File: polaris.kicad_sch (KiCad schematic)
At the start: 17 parts, among them J101 Conn_01x02, J102 Screw_Terminal_01x02, J103 Screw_Terminal_01x02, J104 Screw_Terminal_01x02, J105 Screw_Terminal_01x02, J106 Screw_Terminal_01x02, J107 Screw_Terminal_01x02, J108 Screw_Terminal_01x03, J109 Screw_Terminal_01x03, J110 Screw_Terminal_01x03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

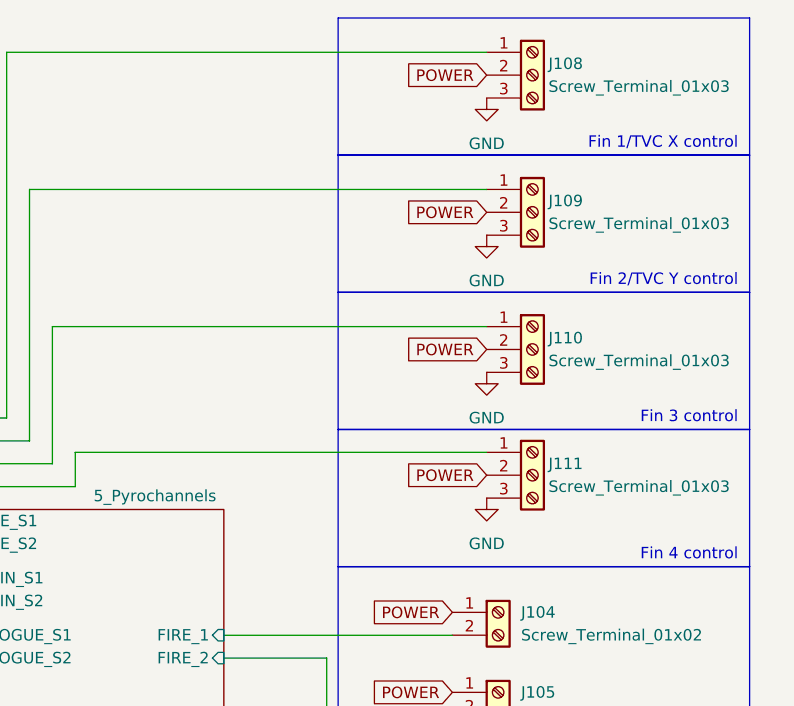
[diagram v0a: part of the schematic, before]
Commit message: Corrected power section for the billionth time Added programming notes
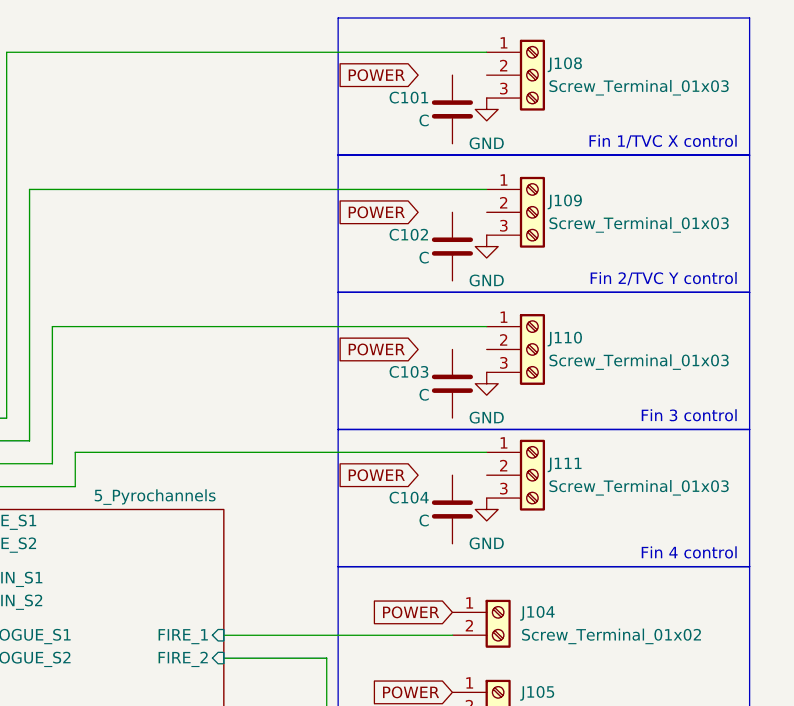
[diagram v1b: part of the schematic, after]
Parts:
- added C101, C102, C103, C104: C, symbol Device:C
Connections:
- net POWER: no longer J108.2 (Pin_2), J109.2 (Pin_2), J110.2 (Pin_2), J111.2 (Pin_2)

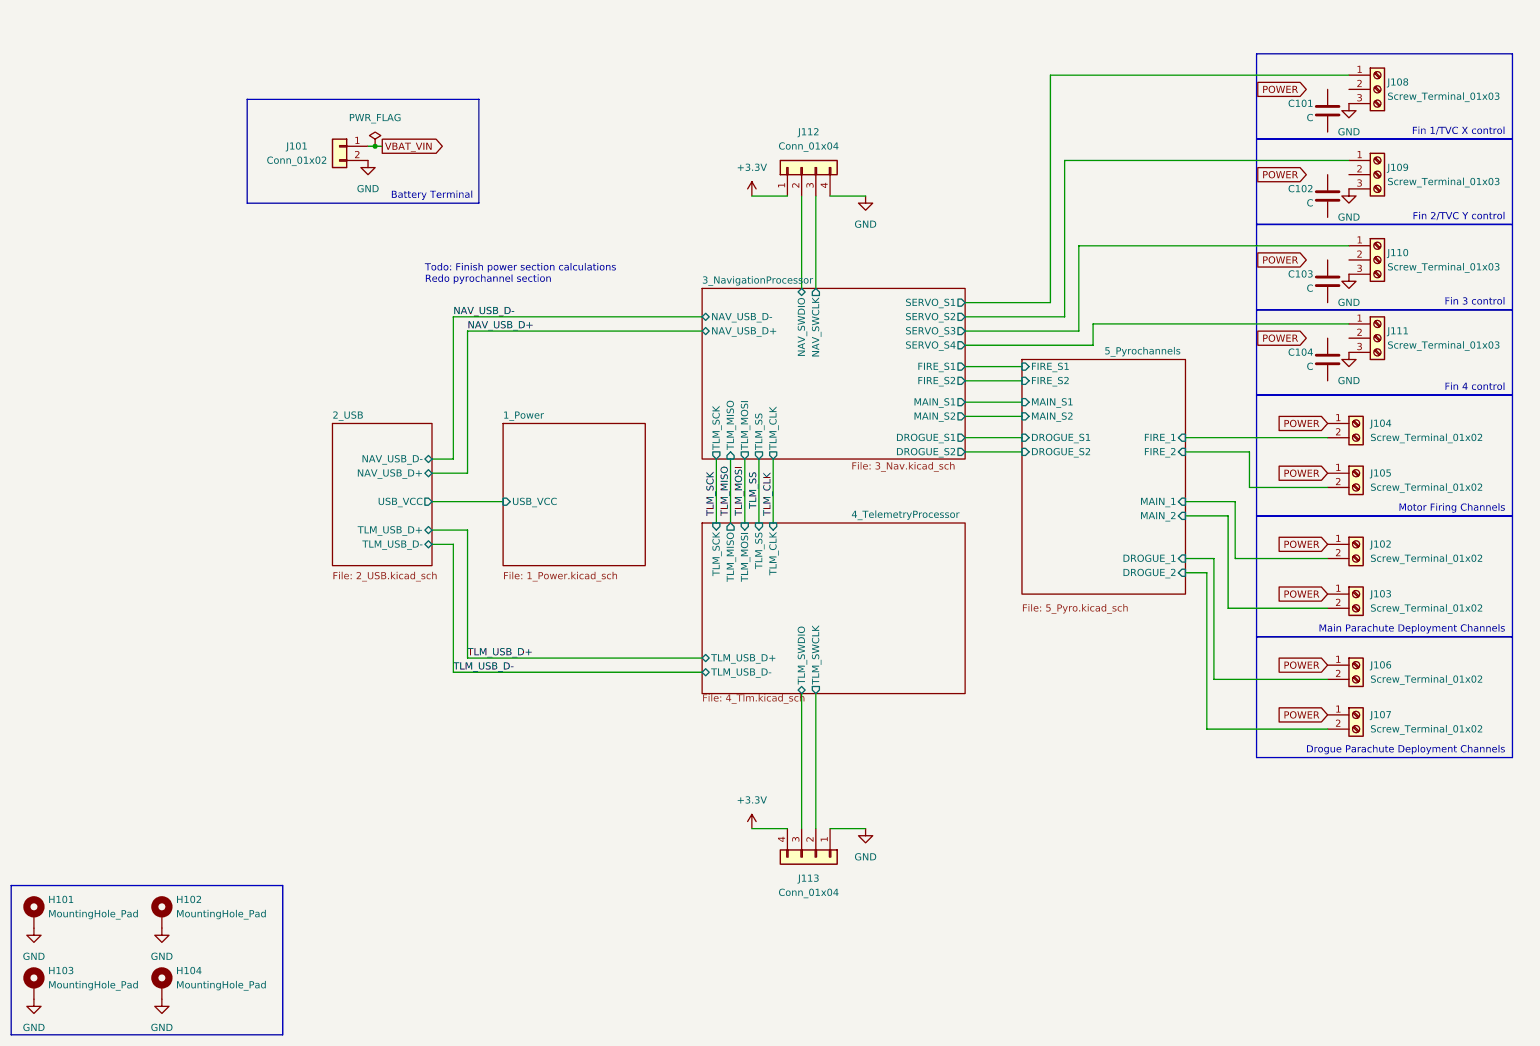
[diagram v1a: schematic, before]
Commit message: Added hardware switch for active control Also added a coupling capacitor between receptacle shells and reference ground Added some more notes
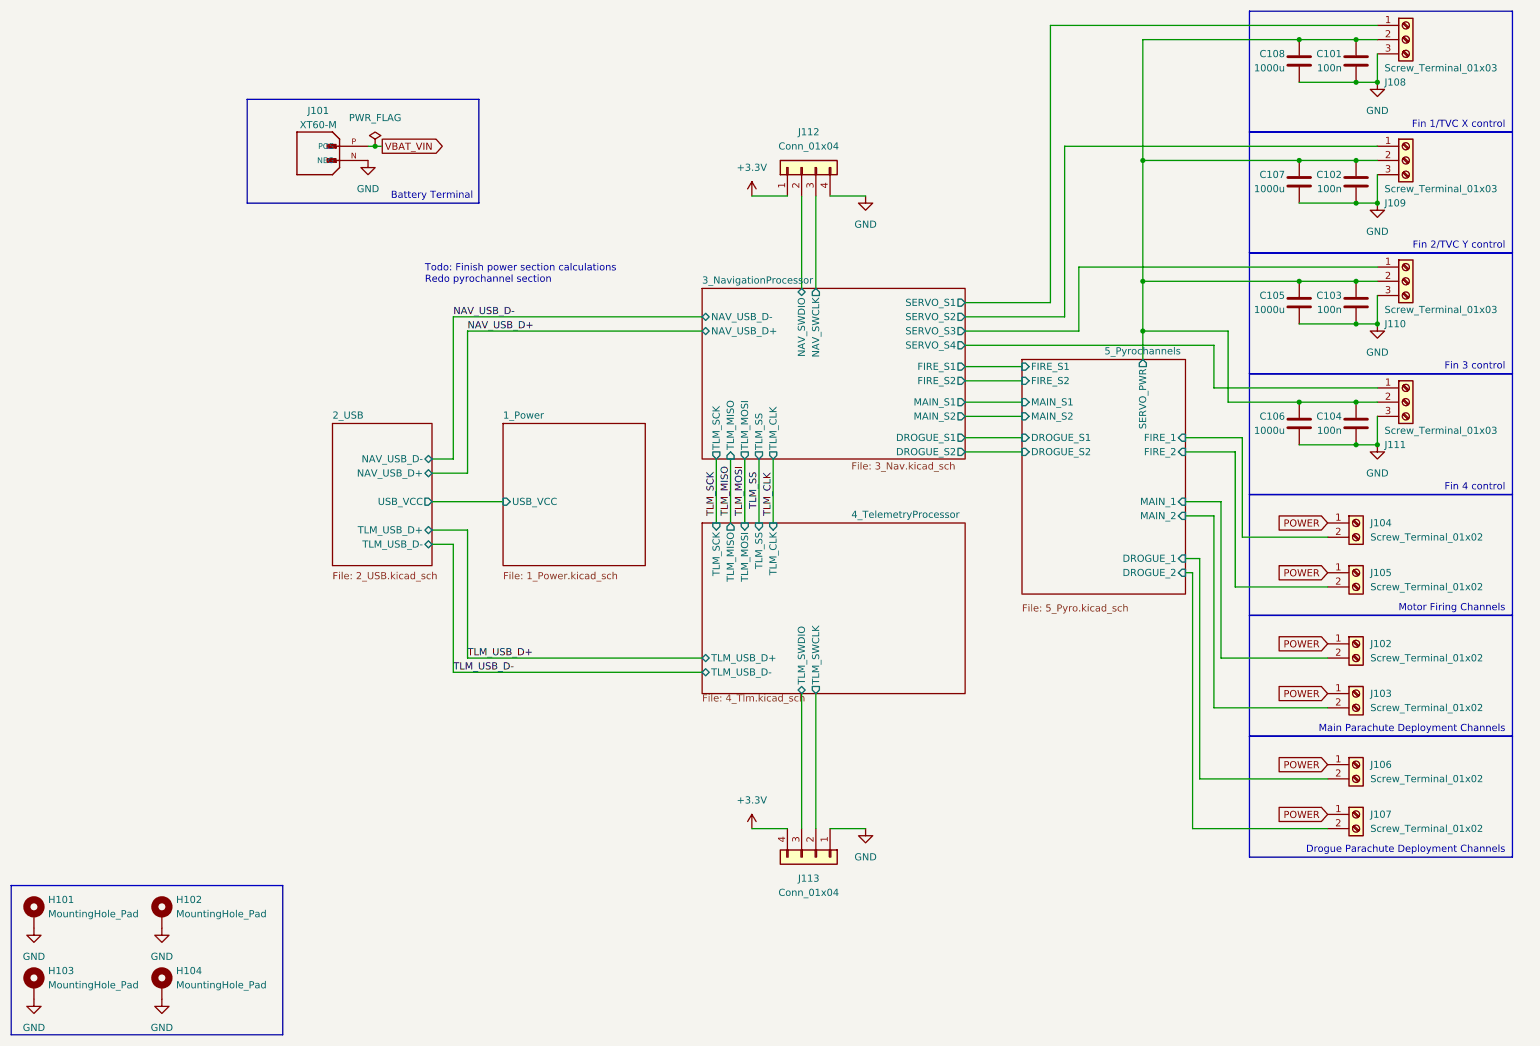
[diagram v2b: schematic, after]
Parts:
- removed J101: Conn_01x02, Connector_AMASS:AMASS_XT60-M_1x02_P7.20mm_Vertical, symbol Connector_Generic:Conn_01x02
- added C105, C106, C107, C108: 1000u, symbol Device:C
- added J101: XT60-M, Connector_AMASS:AMASS_XT60-M_1x02_P7.20mm_Vertical, symbol Polaris_symbols:XT60-M
- C101, C102, C103, C104: value C -> 100n
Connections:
- net GND: now also C101.2, C102.2, C103.2, C104.2, C105.2, C106.2, C107.2, C108.2, J101.N (NEG)
- net VBAT_VIN: now also J101.P (POS)
- net 5_Pyrochannels/SERVO_PWR: now reaches J109.2 (Pin_2)
- net 5_Pyrochannels/SERVO_PWR: now also C101.1, C102.1, C103.1, C104.1, J108.2 (Pin_2), J110.2 (Pin_2), J111.2 (Pin_2), C105.1, C106.1, C107.1, C108.1
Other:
- sheet 5_Pyrochannels ports: added SERVO_PWR; removed none
- title: (none) -> Polaris
- moved on the sheet: C101, C102, C103, C104, J102, J103, J104, J105, J106, J107, J108, J109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

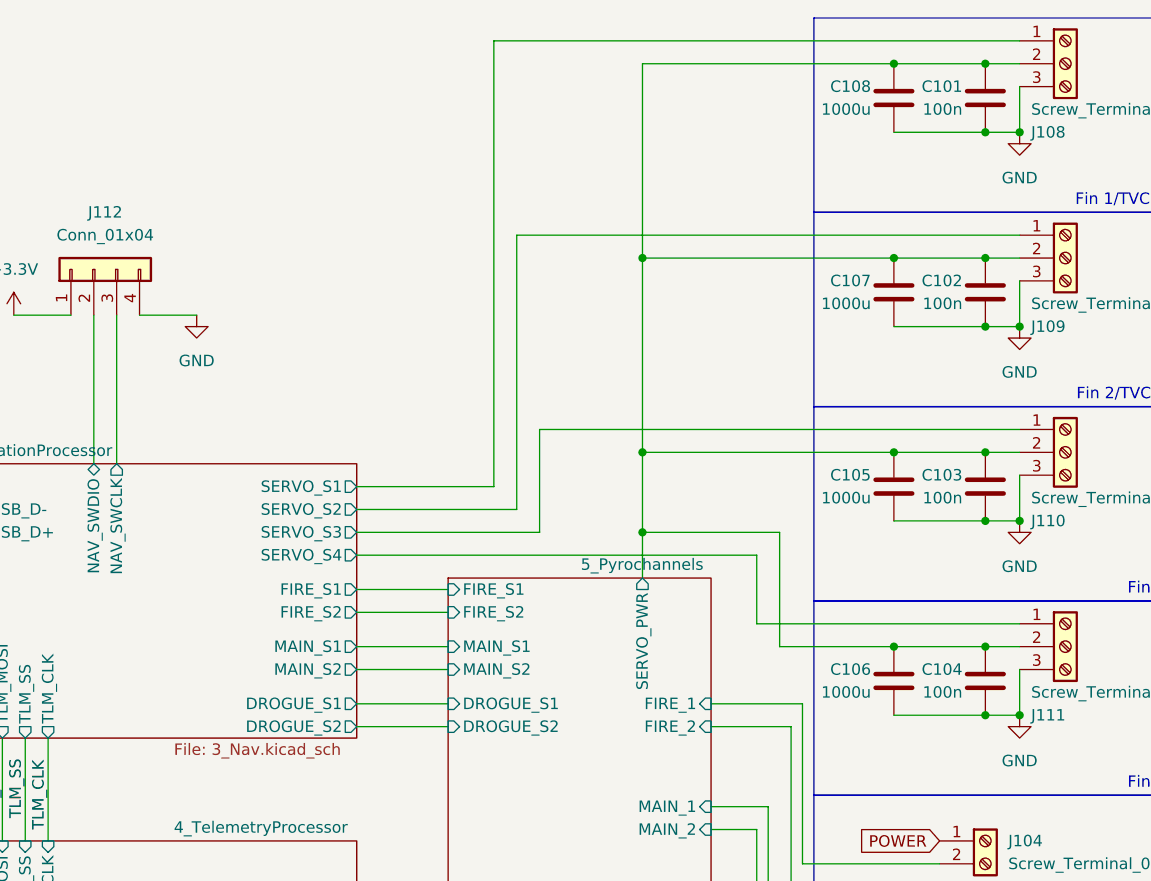
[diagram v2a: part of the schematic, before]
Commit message: Used custom buzzer footprint because why not
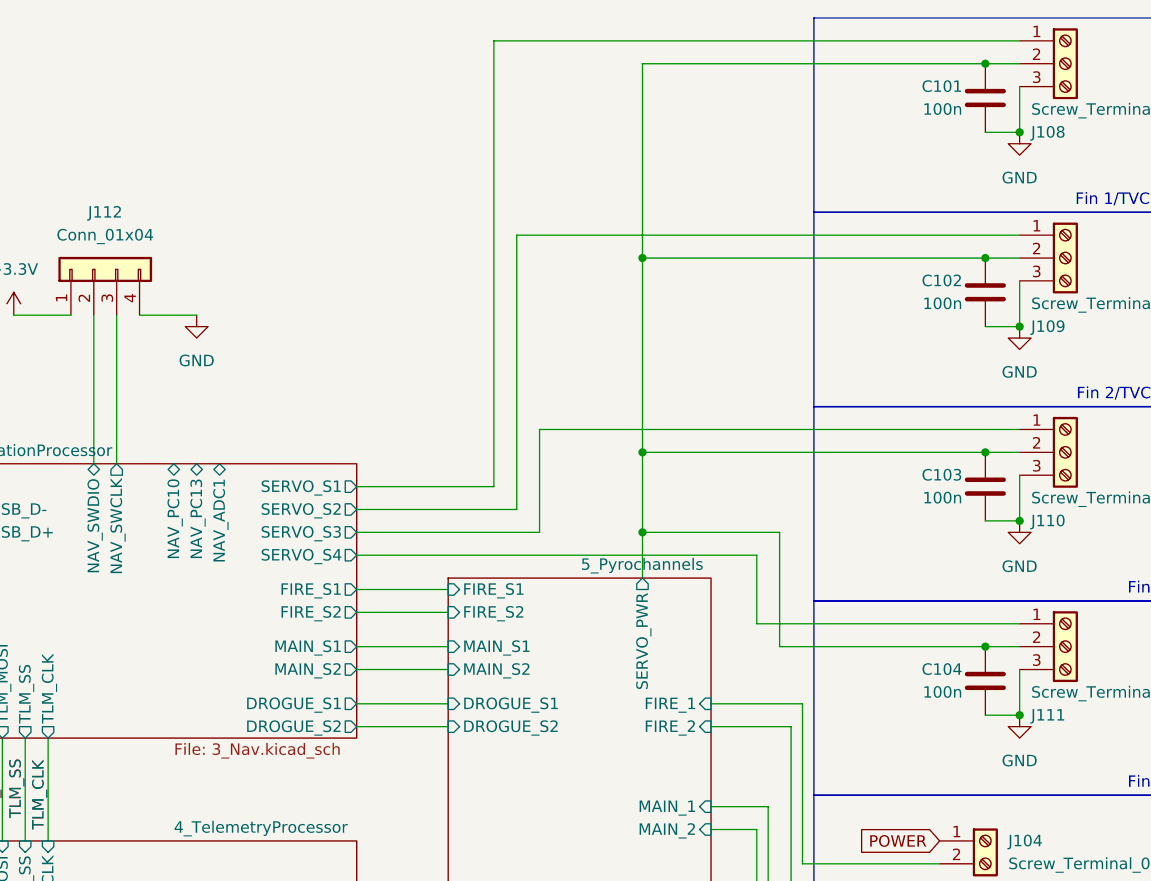
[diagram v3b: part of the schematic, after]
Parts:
- removed C105, C106, C107, C108: 1000u, symbol Device:C
- C101, C102, C103, C104: footprint (none) -> Capacitor_SMD:C_0603_1608Metric
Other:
- sheet 3_NavigationProcessor ports: added NAV_ADC1, NAV_PC10, NAV_PC13; removed none

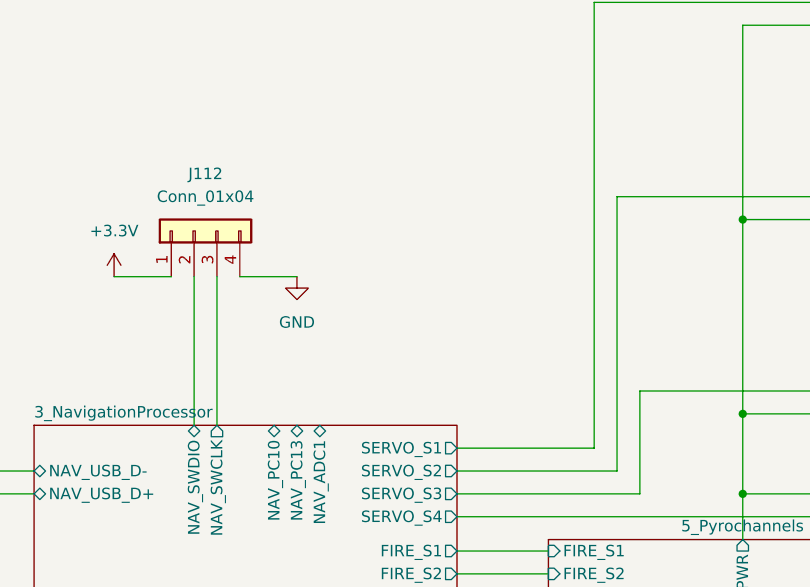
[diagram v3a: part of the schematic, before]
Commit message: Broke out the remaining GPIO pins of NAV
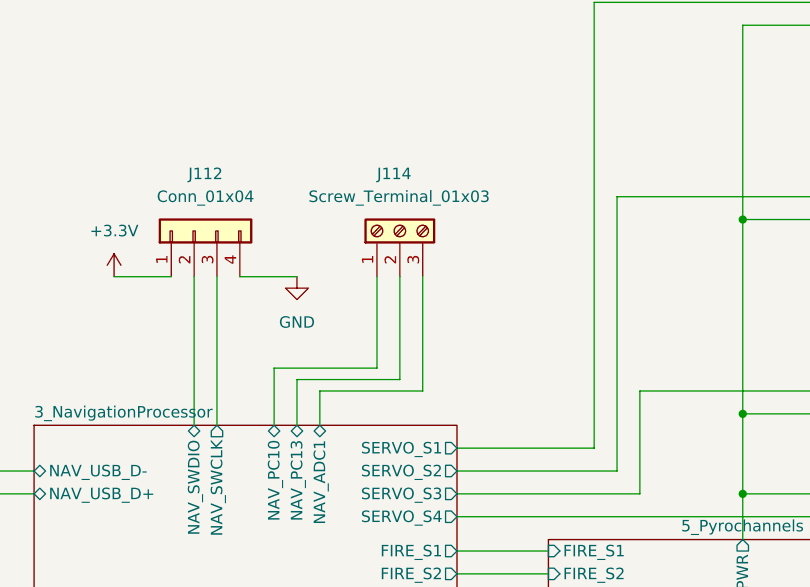
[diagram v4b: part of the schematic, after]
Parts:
- added J114: Screw_Terminal_01x03, TerminalBlock:TerminalBlock_Xinya_XY308-2.54-3P_1x03_P2.54mm_Horizontal, symbol Connector:Screw_Terminal_01x03
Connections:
- net 3_NavigationProcessor/NAV_ADC1: now also J114.3 (Pin_3)
- net 3_NavigationProcessor/NAV_PC10: now also J114.1 (Pin_1)
- net 3_NavigationProcessor/NAV_PC13: now also J114.2 (Pin_2)
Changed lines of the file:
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@@
 	(wire
 		(pts
+			(xy 163.83 57.15) (xy 175.26 57.15)
+		)
+		(stroke
+			(width 0)
+			(type default)
+		)
+	)
+	(wire
+		(pts
 			(xy 92.71 68.58) (xy 92.71 93.98)
 		)
@@
 	(wire
 		(pts
+			(xy 166.37 58.42) (xy 177.8 58.42)
+		)
+		(stroke
+			(width 0)
+			(type default)
+		)
+	)
+	(wire
+		(pts
 			(xy 78.74 38.1) (xy 80.01 38.1)
 		)
@@
 	(wire
 		(pts
+			(xy 168.91 59.69) (xy 180.34 59.69)
+		)
+		(stroke
+			(width 0)
+			(type default)
+		)
+	)
+	(wire
+		(pts
 			(xy 204.47 59.69) (xy 257.81 59.69)
 		)
@@
 	(wire
 		(pts
+			(xy 168.91 63.5) (xy 168.91 59.69)
+		)
+		(stroke
+			(width 0)
+			(type default)
+		)
+	)
+	(wire
+		(pts
 			(xy 223.52 101.6) (xy 229.87 101.6)
 		)
@@
 	(wire
 		(pts
+			(xy 177.8 46.99) (xy 177.8 58.42)
+		)
+		(stroke
+			(width 0)
+			(type default)
+		)
+	)
+	(wire
+		(pts
 			(xy 88.9 101.6) (xy 101.6 101.6)
 		)
@@
 	(wire
 		(pts
+			(xy 163.83 63.5) (xy 163.83 57.15)
+		)
+		(stroke
+			(width 0)
+			(type default)
+		)
+	)
+	(wire
+		(pts
 			(xy 146.05 160.02) (xy 152.4 160.02)
 		)
@@
 	(wire
 		(pts
+			(xy 180.34 59.69) (xy 180.34 46.99)
+		)
+		(stroke
+			(width 0)
+			(type default)
+		)
+	)
+	(wire
+		(pts
 			(xy 254 19.05) (xy 257.81 19.05)
 		)
@@
 	(wire
 		(pts
+			(xy 166.37 63.5) (xy 166.37 58.42)
+		)
+		(stroke
+			(width 0)
+			(type default)
+		)
+	)
+	(wire
+		(pts
 			(xy 184.15 77.47) (xy 194.31 77.47)
 		)
@@
 	(wire
 		(pts
+			(xy 175.26 46.99) (xy 175.26 57.15)
+		)
+		(stroke
+			(width 0)
+			(type default)
+		)
+	)
+	(wire
+		(pts
 			(xy 95.25 106.68) (xy 95.25 129.54)
 		)
@@
 					(unit 1)
 				)
+			)
+		)
+	)
+	(symbol
+		(lib_id "Connector:Screw_Terminal_01x03")
+		(at 177.8 41.91 90)
+		(unit 1)
+		(body_style 1)
+		(exclude_from_sim no)
+		(in_bom yes)
+		(on_board yes)
+		(in_pos_files yes)
+		(dnp no)
+		(property "Reference" "J114"
+			(at 175.26 35.56 90)
+			(show_name no)
+			(do_not_autoplace no)
+			(effects
+				(font
+					(size 1.27 1.27)
+				)
+				(justify right)
+			)
+		)
+		(property "Value" "Screw_Terminal_01x03"
+			(at 167.64 38.1 90)
+			(show_name no)
+			(do_not_autoplace no)
+			(effects
+				(font
+					(size 1.27 1.27)
+				)
+				(justify right)
+			)
+		)
+		(property "Footprint" "TerminalBlock:TerminalBlock_Xinya_XY308-2.54-3P_1x03_P2.54mm_Horizontal"
+			(at 177.8 41.91 0)
+			(hide yes)
+			(show_name no)
+			(do_not_autoplace no)
+			(effects
+				(font
+					(size 1.27 1.27)
+				)
+			)
+		)
+		(property "Datasheet" ""
+			(at 177.8 41.91 0)
+			(hide yes)
+			(show_name no)
+			(do_not_autoplace no)
+			(effects
+				(font
+					(size 1.27 1.27)
+				)
+			)
+		)
+		(property "Description" "Generic screw terminal, single row, 01x03, script generated (kicad-library-utils/schlib/autogen/connector/)"
+			(at 177.8 41.91 0)
+			(hide yes)
+			(show_name no)
+			(do_not_autoplace no)
+			(effects
+				(font
+					(size 1.27 1.27)
+				)
+			)
+		)
+		(pin "2"
+		)
+		(pin "1"
+		)
+		(pin "3"
+		)
+		(instances
+			(project "polaris"
+				(path "/cfb90e19-9fbe-47a1-a5ac-df522853d1d0"
+					(reference "J114")
+					(unit 1)
+				)

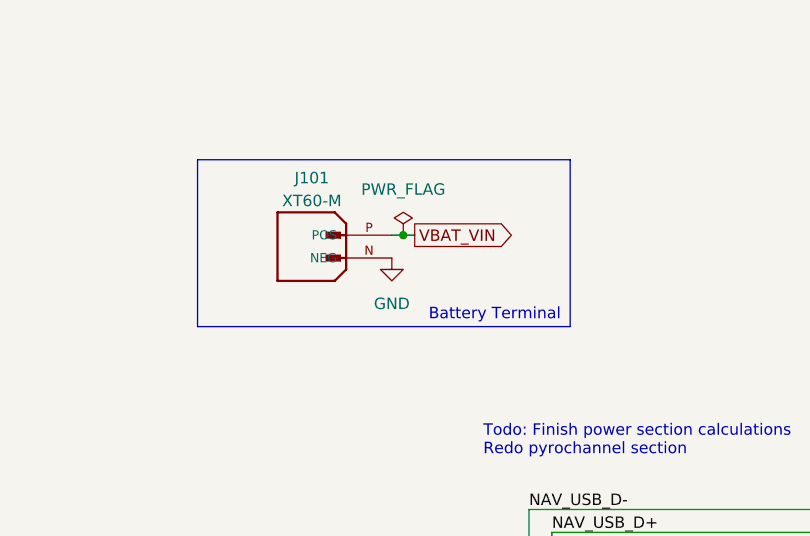
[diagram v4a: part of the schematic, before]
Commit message: Finally started the PCB layout and routing Only took me a few decades Also labeled some unlabeled nets in the schematic Changed the USB mux to be two 1x3 pin headers instead of one 2x3 Edited symbols and footprints to match pin numbers
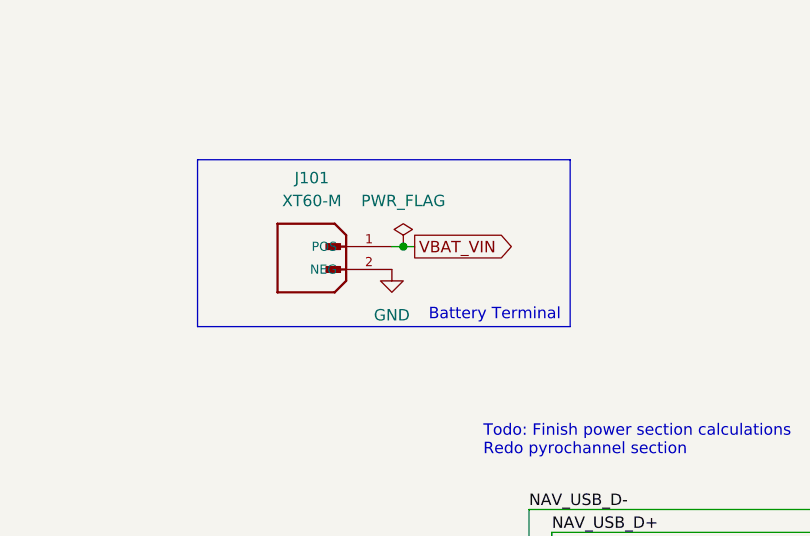
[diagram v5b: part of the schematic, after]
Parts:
- J101: footprint Connector_AMASS:AMASS_XT60-M_1x02_P7.20mm_Vertical -> Connector_AMASS:AMASS_XT60-F_1x02_P7.20mm_Vertical
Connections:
- net GND: now also J101.2 (NEG); no longer J101.N (NEG)
- net VBAT_VIN: now also J101.1 (POS); no longer J101.P (POS)
